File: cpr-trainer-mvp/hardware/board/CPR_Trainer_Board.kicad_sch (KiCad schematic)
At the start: 10 parts, among them J1 ADXL355, J4 ESP32, SW1 SW

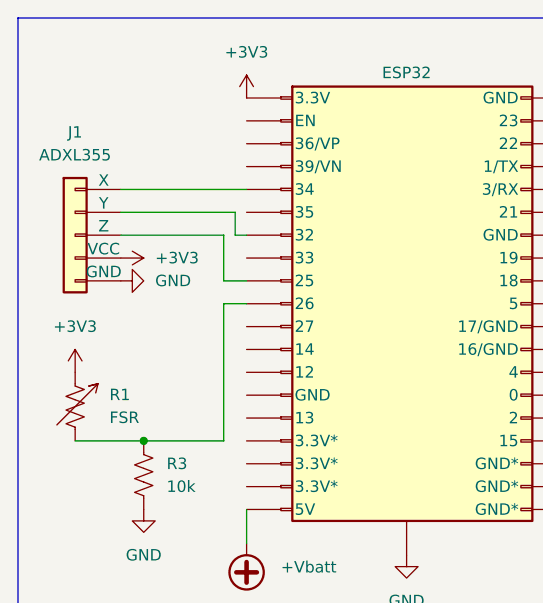
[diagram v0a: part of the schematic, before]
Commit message: Pre-merge README fix, updated GPIO Pins
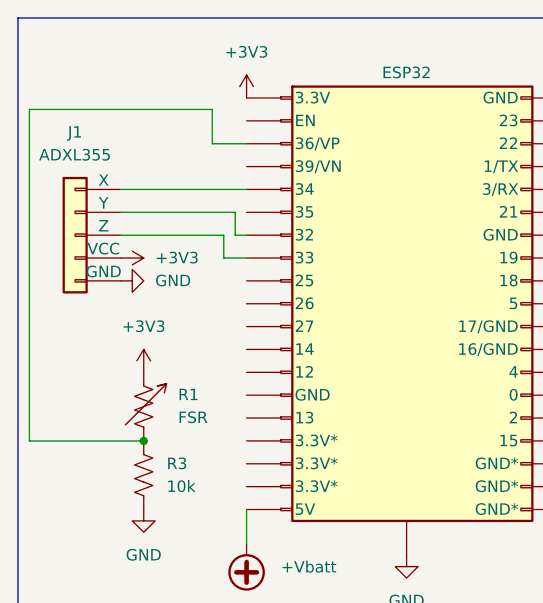
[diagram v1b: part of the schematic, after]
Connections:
- net at R1.2, R3.1: now also J4.3 (36/VP); no longer J4.10 (26)
- net at J1.3 (Z): now also J4.8 (33); no longer J4.9 (25)
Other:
- moved on the sheet: R1
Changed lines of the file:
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@@
+	)
+	(junction
+		(at 81.28 73.66)
+		(diameter 0)
+		(color 0 0 0 0)
+	)
+	(junction
+		(at 81.28 76.2)
+		(diameter 0)
+		(color 0 0 0 0)
 	)
 	(junction
@@
 		(color 0 0 0 0)
 	)
-	(junction
-		(at 81.28 73.66)
-		(diameter 0)
-		(color 0 0 0 0)
-	)
-	(junction
-		(at 81.28 76.2)
-		(diameter 0)
-		(color 0 0 0 0)
-	)
 	(no_connect
 		(at 125.73 25.4)
@@
 	(wire
 		(pts
-			(xy 43.18 45.72) (xy 43.18 50.8)
+			(xy 41.91 31.75) (xy 41.91 35.56)
 		)
 		(stroke
@@
 	(wire
 		(pts
-			(xy 26.67 68.58) (xy 34.29 68.58)
+			(xy 21.59 31.75) (xy 41.91 31.75)
+		)
+		(stroke
+			(width 0)
+			(type default)
+		)
+	)
+	(bus
+		(pts
+			(xy 115.57 21.59) (xy 143.51 21.59)
 		)
 		(stroke
@@
 	(wire
 		(pts
-			(xy 43.18 50.8) (xy 45.72 50.8)
+			(xy 45.72 80.01) (xy 45.72 76.2)
+		)
+		(stroke
+			(width 0)
+			(type default)
+		)
+	)
+	(wire
+		(pts
+			(xy 31.75 45.72) (xy 43.18 45.72)
 		)
 		(stroke
@@
 	(bus
 		(pts
-			(xy 115.57 21.59) (xy 143.51 21.59)
+			(xy 135.89 88.9) (xy 115.57 88.9)
+		)
+		(stroke
+			(width 0)
+			(type default)
+		)
+	)
+	(bus
+		(pts
+			(xy 20.32 21.59) (xy 20.32 88.9)
 		)
 		(stroke
@@
 	(wire
 		(pts
-			(xy 45.72 80.01) (xy 45.72 76.2)
+			(xy 43.18 45.72) (xy 43.18 48.26)
 		)
 		(stroke
@@
 	(wire
 		(pts
-			(xy 31.75 45.72) (xy 43.18 45.72)
+			(xy 44.45 45.72) (xy 45.72 45.72)
 		)
 		(stroke
@@
 	(bus
 		(pts
-			(xy 135.89 88.9) (xy 115.57 88.9)
+			(xy 20.32 21.59) (xy 109.22 21.59)
 		)
 		(stroke
@@
 	(bus
 		(pts
-			(xy 20.32 21.59) (xy 20.32 88.9)
+			(xy 115.57 21.59) (xy 115.57 41.91)
+		)
+		(stroke
+			(width 0)
+			(type default)
+		)
+	)
+	(bus
+		(pts
+			(xy 143.51 21.59) (xy 143.51 41.91)
 		)
 		(stroke
@@
 	(wire
 		(pts
-			(xy 44.45 45.72) (xy 45.72 45.72)
+			(xy 43.18 48.26) (xy 45.72 48.26)
 		)
 		(stroke
@@
 	(wire
 		(pts
-			(xy 43.18 53.34) (xy 43.18 68.58)
+			(xy 31.75 43.18) (xy 44.45 43.18)
+		)
+		(stroke
+			(width 0)
+			(type default)
+		)
+	)
+	(wire
+		(pts
+			(xy 31.75 40.64) (xy 45.72 40.64)
 		)
 		(stroke
@@
 	(bus
 		(pts
-			(xy 20.32 21.59) (xy 109.22 21.59)
+			(xy 115.57 60.96) (xy 135.89 60.96)
+		)
+		(stroke
+			(width 0)
+			(type default)
+		)
+	)
+	(wire
+		(pts
+			(xy 21.59 31.75) (xy 21.59 68.58)
 		)
 		(stroke
@@
 	(bus
 		(pts
-			(xy 115.57 21.59) (xy 115.57 41.91)
+			(xy 143.51 41.91) (xy 115.57 41.91)
 		)
 		(stroke
@@
 	(bus
 		(pts
-			(xy 143.51 21.59) (xy 143.51 41.91)
+			(xy 109.22 21.59) (xy 109.22 88.9)
 		)
 		(stroke
@@
 	(wire
 		(pts
-			(xy 31.75 43.18) (xy 44.45 43.18)
+			(xy 81.28 71.12) (xy 81.28 73.66)
+		)
+		(stroke
+			(width 0)
+			(type default)
+		)
+	)
+	(bus
+		(pts
+			(xy 109.22 88.9) (xy 20.32 88.9)
 		)
 		(stroke
@@
 	(wire
 		(pts
-			(xy 31.75 40.64) (xy 45.72 40.64)
+			(xy 100.33 48.26) (xy 100.33 52.07)
+		)
+		(stroke
+			(width 0)
+			(type default)
+		)
+	)
+	(wire
+		(pts
+			(xy 81.28 73.66) (xy 81.28 76.2)
+		)
+		(stroke
+			(width 0)
+			(type default)
+		)
+	)
+	(wire
+		(pts
+			(xy 81.28 76.2) (xy 81.28 81.28)
 		)
 		(stroke
@@
 	(bus
 		(pts
-			(xy 115.57 60.96) (xy 135.89 60.96)
-		)
-		(stroke
-			(width 0)
-			(type default)
-		)
-	)
-	(bus
-		(pts
-			(xy 143.51 41.91) (xy 115.57 41.91)
-		)
-		(stroke
-			(width 0)
-			(type default)
-		)
-	)
-	(bus
-		(pts
-			(xy 109.22 21.59) (xy 109.22 88.9)
+			(xy 135.89 60.96) (xy 135.89 88.9)
 		)
 		(stroke
@@
 	(wire
 		(pts
-			(xy 81.28 71.12) (xy 81.28 73.66)
-		)
-		(stroke
-			(width 0)
-			(type default)
-		)
-	)
-	(bus
-		(pts
-			(xy 109.22 88.9) (xy 20.32 88.9)
+			(xy 21.59 68.58) (xy 34.29 68.58)
 		)
 		(stroke
@@
 	(wire
 		(pts
-			(xy 100.33 48.26) (xy 100.33 52.07)
+			(xy 100.33 63.5) (xy 100.33 62.23)
 		)
 		(stroke
@@
 	(wire
 		(pts
-			(xy 34.29 68.58) (xy 43.18 68.58)
+			(xy 81.28 50.8) (xy 88.9 50.8)
 		)
 		(stroke
@@
 	(wire
 		(pts
-			(xy 81.28 73.66) (xy 81.28 76.2)
+			(xy 44.45 43.18) (xy 44.45 45.72)
 		)
 		(stroke
@@
 	(wire
 		(pts
-			(xy 81.28 76.2) (xy 81.28 81.28)
+			(xy 100.33 44.45) (xy 100.33 48.26)
 		)
 		(stroke
@@
 	(wire
 		(pts
-			(xy 43.18 53.34) (xy 45.72 53.34)
-		)
-		(stroke
-			(width 0)
-			(type default)
-		)
-	)
-	(bus
-		(pts
-			(xy 135.89 60.96) (xy 135.89 88.9)
+			(xy 81.28 48.26) (xy 100.33 48.26)
 		)
 		(stroke
@@
 	(wire
 		(pts
-			(xy 100.33 63.5) (xy 100.33 62.23)
-		)
-		(stroke
-			(width 0)
-			(type default)
-		)
-	)
-	(wire
-		(pts
-			(xy 81.28 50.8) (xy 88.9 50.8)
-		)
-		(stroke
-			(width 0)
-			(type default)
-		)
-	)
-	(wire
-		(pts
-			(xy 44.45 43.18) (xy 44.45 45.72)
-		)
-		(stroke
-			(width 0)
-			(type default)
-		)
-	)
-	(wire
-		(pts
-			(xy 100.33 44.45) (xy 100.33 48.26)
-		)
-		(stroke
-			(width 0)
-			(type default)
-		)
-	)
-	(wire
-		(pts
-			(xy 81.28 48.26) (xy 100.33 48.26)
+			(xy 41.91 35.56) (xy 45.72 35.56)
 		)
 		(stroke
@@
 	(symbol
 		(lib_id "Device:R_Variable_US")
-		(at 26.67 64.77 0)
+		(at 34.29 64.77 0)
 		(unit 1)
 		(body_style 1)
@@
 		(fields_autoplaced yes)
 		(property "Reference" "R1"
-			(at 30.48 63.4618 0)
+			(at 38.1 63.4618 0)
 			(show_name no)
 			(do_not_autoplace no)
@@
 		)
 		(property "Value" "FSR"
-			(at 30.48 66.0018 0)
+			(at 38.1 66.0018 0)
 			(show_name no)
 			(do_not_autoplace no)
@@
 		)
 		(property "Footprint" ""
-			(at 24.892 64.77 90)
+			(at 32.512 64.77 90)
 			(hide yes)
 			(show_name no)
@@
 		)
 		(property "Datasheet" ""
-			(at 26.67 64.77 0)
+			(at 34.29 64.77 0)
 			(hide yes)
 			(show_name no)
@@
 		)
 		(property "Description" "Variable resistor, US symbol"
-			(at 26.67 64.77 0)
+			(at 34.29 64.77 0)
 			(hide yes)
 			(show_name no)
@@
 	(symbol
 		(lib_id "power:+3V3")
-		(at 26.67 60.96 0)
+		(at 34.29 60.96 0)
 		(unit 1)
 		(body_style 1)
@@
 		(fields_autoplaced yes)
 		(property "Reference" "#PWR07"
-			(at 26.67 64.77 0)
+			(at 34.29 64.77 0)
 			(hide yes)
 			(show_name no)
@@
 		)
 		(property "Value" "+3V3"
-			(at 26.67 55.88 0)
+			(at 34.29 55.88 0)
 			(show_name no)
 			(do_not_autoplace no)
@@
 		)
 		(property "Footprint" ""
-			(at 26.67 60.96 0)
+			(at 34.29 60.96 0)
 			(hide yes)
 			(show_name no)
@@
 		)
 		(property "Datasheet" ""
-			(at 26.67 60.96 0)
+			(at 34.29 60.96 0)
 			(hide yes)
 			(show_name no)
@@
 		)
 		(property "Description" "Power symbol creates a global label with name \"+3V3\""
-			(at 26.67 60.96 0)
-			(hide yes)
-			(show_name no)
+			(at 34.29 60.96 0)
+			(hide yes)
+			(show_name no)
